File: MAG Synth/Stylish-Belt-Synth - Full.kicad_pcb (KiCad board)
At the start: 2 copper layers, 177.8 x 101.7 mm, 42 parts, among them J1 Conn_01x06, J26 WRITE PATCH, J27 PARAM SELECT, J28 PATCH SELECT, J29 MODE, J30 STYLUS, SW1 Power, U1 stm32f103c8t6-module-china_smd, U2 XPT8871

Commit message: Code now lets you play music!
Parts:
- LS1: footprint Pin_Headers:Pin_Header_Angled_1x02_Pitch2.54mm -> Pin_Headers:Pin_Header_Straight_1x02_Pitch2.54mm
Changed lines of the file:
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@@
   (general
     (thickness 1.6)
-    (drawings 148)
+    (drawings 150)
     (tracks 1041)
     (zones 0)
@@
     (37 F.SilkS user)
     (38 B.Mask user)
-    (39 F.Mask user hide)
+    (39 F.Mask user)
     (40 Dwgs.User user)
     (41 Cmts.User user)
@@
   )
   (setup
-    (last_trace_width 0.762)
+    (last_trace_width 0.508)
     (user_trace_width 0.381)
     (user_trace_width 0.508)
@@
     (add_net "Net-(U1-Pad38)")
   )
+  (module Pin_Headers:Pin_Header_Straight_1x02_Pitch2.54mm (layer F.Cu)
+    (at 196.215 87.63 180)
+    (descr "Through hole straight pin header, 1x02, 2.54mm pitch, single row")
+    (tags "Through hole pin header THT 1x02 2.54mm single row")
+    (fp_text reference LS1 (at 2.54 1.27 90) (layer B.SilkS)
+      (effects (font (size 1 1) (thickness 0.15)) (justify mirror))
+    )
+    (fp_text value Speaker (at 2.54 -3.81 180) (layer B.Fab)
+      (effects (font (size 1.499997 1.499997) (thickness 0.15)) (justify mirror))
+    )
+    (fp_line (start -0.635 -1.27) (end 1.27 -1.27) (layer F.Fab) (width 0.1))
+    (fp_line (start 1.27 -1.27) (end 1.27 3.81) (layer F.Fab) (width 0.1))
+    (fp_line (start 1.27 3.81) (end -1.27 3.81) (layer F.Fab) (width 0.1))
+    (fp_line (start -1.27 3.81) (end -1.27 -0.635) (layer F.Fab) (width 0.1))
+    (fp_line (start -1.27 -0.635) (end -0.635 -1.27) (layer F.Fab) (width 0.1))
+    (fp_line (start -1.33 3.87) (end 1.33 3.87) (layer F.SilkS) (width 0.12))
+    (fp_line (start -1.33 1.27) (end -1.33 3.87) (layer F.SilkS) (width 0.12))
+    (fp_line (start 1.33 1.27) (end 1.33 3.87) (layer F.SilkS) (width 0.12))
+    (fp_line (start -1.33 1.27) (end 1.33 1.27) (layer F.SilkS) (width 0.12))
+    (fp_line (start -1.33 0) (end -1.33 -1.33) (layer F.SilkS) (width 0.12))
+    (fp_line (start -1.33 -1.33) (end 0 -1.33) (layer F.SilkS) (width 0.12))
+    (fp_line (start -1.8 -1.8) (end -1.8 4.35) (layer F.CrtYd) (width 0.05))
+    (fp_line (start -1.8 4.35) (end 1.8 4.35) (layer F.CrtYd) (width 0.05))
+    (fp_line (start 1.8 4.35) (end 1.8 -1.8) (layer F.CrtYd) (width 0.05))
+    (fp_line (start 1.8 -1.8) (end -1.8 -1.8) (layer F.CrtYd) (width 0.05))
+    (fp_text user %R (at 2.77 1.27 90) (layer B.Fab)
+      (effects (font (size 1 1) (thickness 0.15)) (justify mirror))
+    )
+    (pad 1 thru_hole rect (at 0 0 180) (size 1.7 1.7) (drill 1) (layers *.Cu *.Mask)
+      (net 50 /XH-M125-amp-board/OUT+))
+    (pad 2 thru_hole oval (at 0 2.54 180) (size 1.7 1.7) (drill 1) (layers *.Cu *.Mask)
+      (net 48 /XH-M125-amp-board/OUT-))
+    (model ${KISYS3DMOD}/Pin_Headers.3dshapes/Pin_Header_Straight_1x02_Pitch2.54mm.wrl
+      (at (xyz 0 0 0))
+      (scale (xyz 1 1 1))
+      (rotate (xyz 0 0 0))
+    )
+  )
   (module SoftEggKiCAD:LargeRoundTouchPad (layer B.Cu)
     (at 90.932 140.208)
@@
     )
   )
-  (module Pin_Headers:Pin_Header_Angled_1x02_Pitch2.54mm (layer F.Cu)
-    (at 196.215 87.63 180)
-    (descr "Through hole angled pin header, 1x02, 2.54mm pitch, 6mm pin length, single row")
-    (tags "Through hole angled pin header THT 1x02 2.54mm single row")
-    (fp_text reference LS1 (at 2.54 1.27 90) (layer B.SilkS)
-      (effects (font (size 1 1) (thickness 0.15)) (justify mirror))
-    )
-    (fp_text value Speaker (at 2.54 -3.81 180) (layer B.Fab)
-      (effects (font (size 1.499997 1.499997) (thickness 0.15)) (justify mirror))
-    )
-    (fp_line (start 2.135 -1.27) (end 4.04 -1.27) (layer F.Fab) (width 0.1))
-    (fp_line (start 4.04 -1.27) (end 4.04 3.81) (layer F.Fab) (width 0.1))
-    (fp_line (start 4.04 3.81) (end 1.5 3.81) (layer F.Fab) (width 0.1))
-    (fp_line (start 1.5 3.81) (end 1.5 -0.635) (layer F.Fab) (width 0.1))
-    (fp_line (start 1.5 -0.635) (end 2.135 -1.27) (layer F.Fab) (width 0.1))
-    (fp_line (start -0.32 -0.32) (end 1.5 -0.32) (layer F.Fab) (width 0.1))
-    (fp_line (start -0.32 -0.32) (end -0.32 0.32) (layer F.Fab) (width 0.1))
-    (fp_line (start -0.32 0.32) (end 1.5 0.32) (layer F.Fab) (width 0.1))
-    (fp_line (start 4.04 -0.32) (end 10.04 -0.32) (layer F.Fab) (width 0.1))
-    (fp_line (start 10.04 -0.32) (end 10.04 0.32) (layer F.Fab) (width 0.1))
-    (fp_line (start 4.04 0.32) (end 10.04 0.32) (layer F.Fab) (width 0.1))
-    (fp_line (start -0.32 2.22) (end 1.5 2.22) (layer F.Fab) (width 0.1))
-    (fp_line (start -0.32 2.22) (end -0.32 2.86) (layer F.Fab) (width 0.1))
-    (fp_line (start -0.32 2.86) (end 1.5 2.86) (layer F.Fab) (width 0.1))
-    (fp_line (start 4.04 2.22) (end 10.04 2.22) (layer F.Fab) (width 0.1))
-    (fp_line (start 10.04 2.22) (end 10.04 2.86) (layer F.Fab) (width 0.1))
-    (fp_line (start 4.04 2.86) (end 10.04 2.86) (layer F.Fab) (width 0.1))
-    (fp_line (start 1.44 -1.33) (end 1.44 3.87) (layer F.SilkS) (width 0.12))
-    (fp_line (start 1.44 3.87) (end 4.1 3.87) (layer F.SilkS) (width 0.12))
-    (fp_line (start 4.1 3.87) (end 4.1 -1.33) (layer F.SilkS) (width 0.12))
-    (fp_line (start 4.1 -1.33) (end 1.44 -1.33) (layer F.SilkS) (width 0.12))
-    (fp_line (start 4.1 -0.38) (end 10.1 -0.38) (layer F.SilkS) (width 0.12))
-    (fp_line (start 10.1 -0.38) (end 10.1 0.38) (layer F.SilkS) (width 0.12))
-    (fp_line (start 10.1 0.38) (end 4.1 0.38) (layer F.SilkS) (width 0.12))
-    (fp_line (start 4.1 -0.32) (end 10.1 -0.32) (layer F.SilkS) (width 0.12))
-    (fp_line (start 4.1 -0.2) (end 10.1 -0.2) (layer F.SilkS) (width 0.12))
-    (fp_line (start 4.1 -0.08) (end 10.1 -0.08) (layer F.SilkS) (width 0.12))
-    (fp_line (start 4.1 0.04) (end 10.1 0.04) (layer F.SilkS) (width 0.12))
-    (fp_line (start 4.1 0.16) (end 10.1 0.16) (layer F.SilkS) (width 0.12))
-    (fp_line (start 4.1 0.28) (end 10.1 0.28) (layer F.SilkS) (width 0.12))
-    (fp_line (start 1.11 -0.38) (end 1.44 -0.38) (layer F.SilkS) (width 0.12))
-    (fp_line (start 1.11 0.38) (end 1.44 0.38) (layer F.SilkS) (width 0.12))
-    (fp_line (start 1.44 1.27) (end 4.1 1.27) (layer F.SilkS) (width 0.12))
-    (fp_line (start 4.1 2.16) (end 10.1 2.16) (layer F.SilkS) (width 0.12))
-    (fp_line (start 10.1 2.16) (end 10.1 2.92) (layer F.SilkS) (width 0.12))
-    (fp_line (start 10.1 2.92) (end 4.1 2.92) (layer F.SilkS) (width 0.12))
-    (fp_line (start 1.042929 2.16) (end 1.44 2.16) (layer F.SilkS) (width 0.12))
-    (fp_line (start 1.042929 2.92) (end 1.44 2.92) (layer F.SilkS) (width 0.12))
-    (fp_line (start -1.27 0) (end -1.27 -1.27) (layer F.SilkS) (width 0.12))
-    (fp_line (start -1.27 -1.27) (end 0 -1.27) (layer F.SilkS) (width 0.12))
-    (fp_line (start -1.8 -1.8) (end -1.8 4.35) (layer F.CrtYd) (width 0.05))
-    (fp_line (start -1.8 4.35) (end 10.55 4.35) (layer F.CrtYd) (width 0.05))
-    (fp_line (start 10.55 4.35) (end 10.55 -1.8) (layer F.CrtYd) (width 0.05))
-    (fp_line (start 10.55 -1.8) (end -1.8 -1.8) (layer F.CrtYd) (width 0.05))
-    (fp_text user %R (at 2.77 1.27 90) (layer B.Fab)
-      (effects (font (size 1 1) (thickness 0.15)) (justify mirror))
-    )
-    (pad 1 thru_hole rect (at 0 0 180) (size 1.7 1.7) (drill 1) (layers *.Cu *.Mask)
-      (net 50 /XH-M125-amp-board/OUT+))
-    (pad 2 thru_hole oval (at 0 2.54 180) (size 1.7 1.7) (drill 1) (layers *.Cu *.Mask)
-      (net 48 /XH-M125-amp-board/OUT-))
-    (model ${KISYS3DMOD}/Pin_Headers.3dshapes/Pin_Header_Angled_1x02_Pitch2.54mm.wrl
-      (offset (xyz 0.127 -2.54 -1.6764))
-      (scale (xyz 1 1 1))
-      (rotate (xyz 180 0 0))
-    )
-  )
   (module WS2812B (layer F.Cu)
     (at 123.825 96.139 202.5)
@@
     (descr "<b>Intelligent control LED with integrated light source</b><p>WS2812B<br>source: http://www.world-semi.com/uploads/soft/130904/1_1500205981.pdf")
     (attr smd)
-    (fp_text reference D0 (at 6.307 -1.71371 90) (layer F.SilkS)
+    (fp_text reference D0 (at 2.4003 -3.556 90) (layer F.SilkS)
       (effects (font (size 0.802674 0.802674) (thickness 0.05)))
     )
-    (fp_text value WS2812B (at 5.78549 1.29688 90) (layer F.SilkS)
+    (fp_text value WS2812B (at 4.0259 -0.0381 180) (layer F.SilkS)
       (effects (font (size 0.480622 0.480622) (thickness 0.05)))
     )
@@
       (xy 6.050594 -4.164124)) (layer F.SilkS) (width 0.01))
   )
+  (gr_text Stylish! (at 189.6364 67.1957) (layer F.Mask)
+    (effects (font (size 5.08 5.08) (thickness 1.27)))
+  )
+  (gr_text Stylish! (at 189.4586 66.9544) (layer F.SilkS)
+    (effects (font (size 5.08 5.08) (thickness 0.762)))
+  )
   (gr_text MODE (at 111.125 88.9) (layer F.Mask)
     (effects (font (size 1.5 1.5) (thickness 0.3)))
@@
     (effects (font (size 1.5 1.5) (thickness 0.3)))
   )
-  (gr_text GND (at 180.975 59.69) (layer F.Cu)
+  (gr_text GND (at 175.5013 59.8043) (layer F.Cu)
     (effects (font (size 1.5 1.5) (thickness 0.3)))
   )

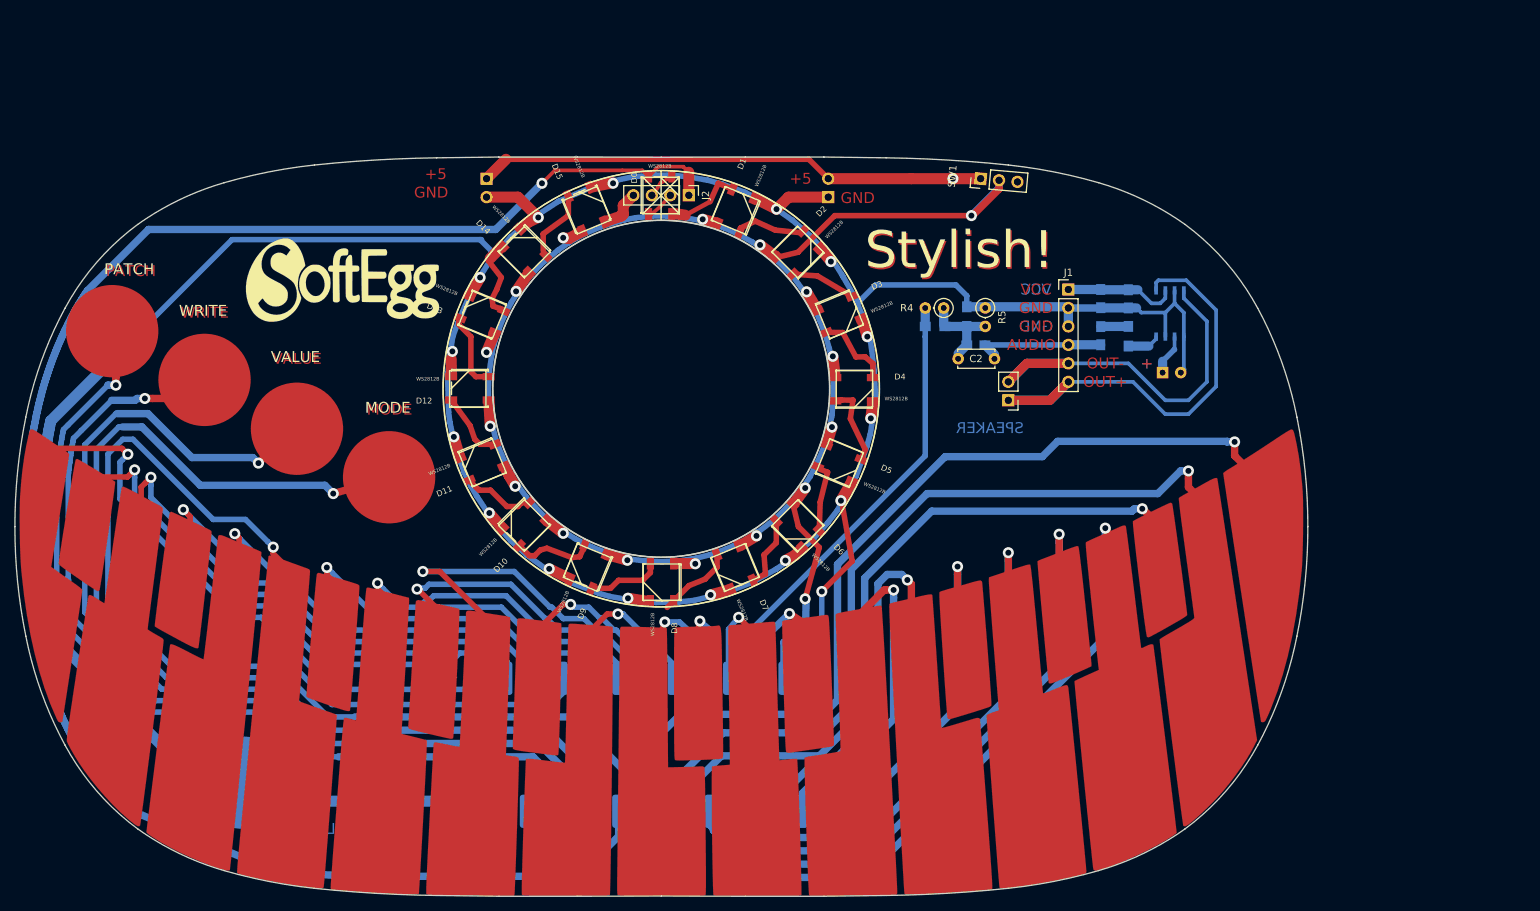
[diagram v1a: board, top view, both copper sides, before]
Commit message: 1st draft of case. Updates to PCB for battery holder mounting and other stuff. Gerbers added for Tindie. Updates to source code, although I don't know if they are the in progress state machine updates or not.
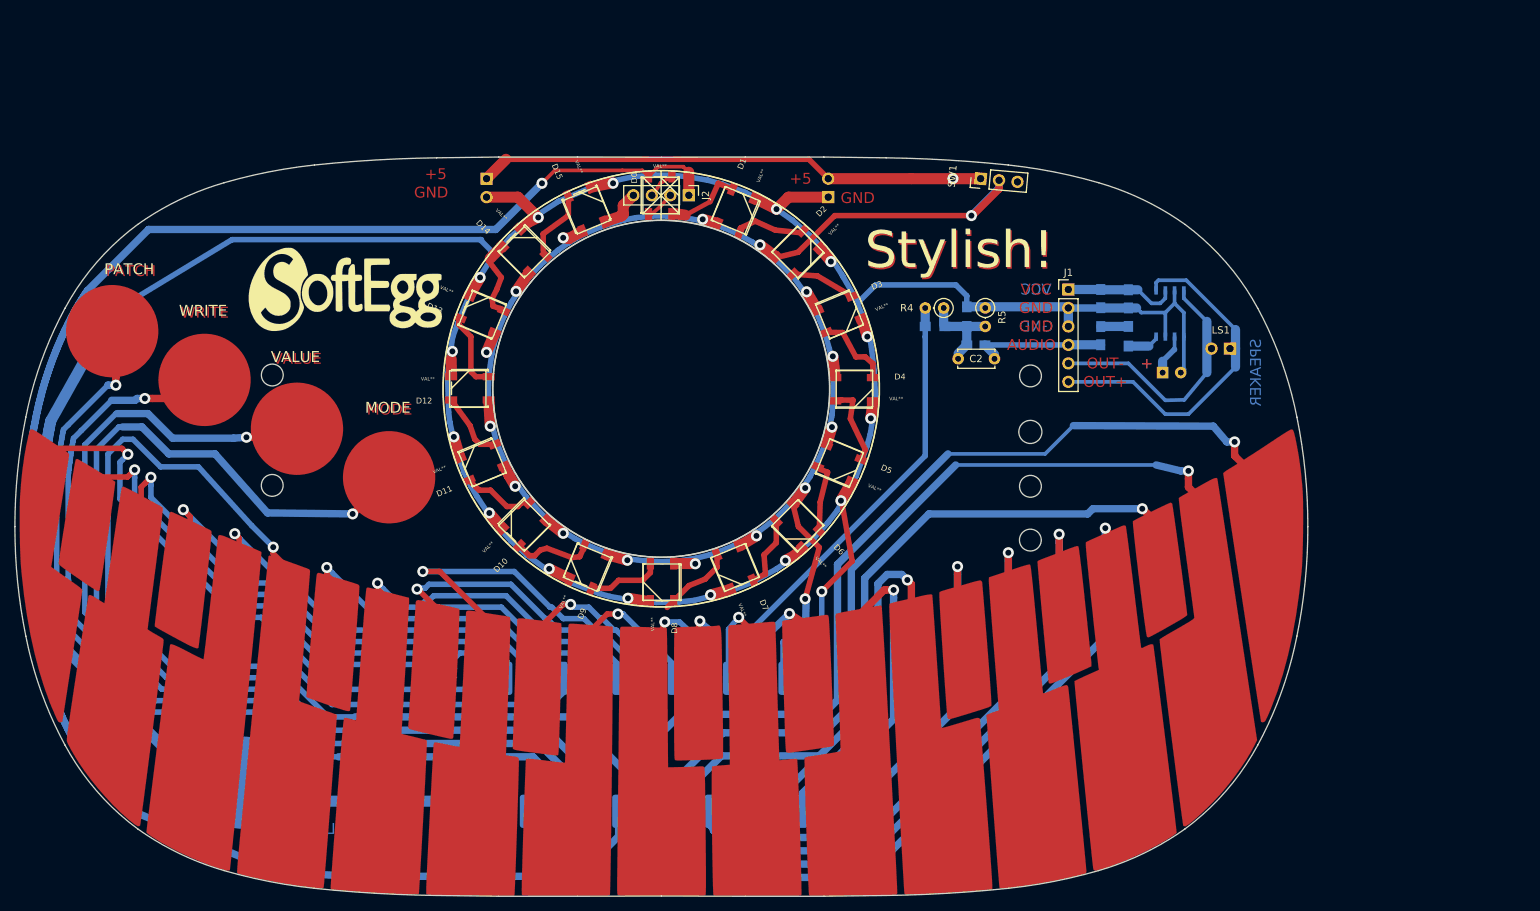
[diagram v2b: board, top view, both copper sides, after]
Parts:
- added REF**: AA Battery Holder, SoftEggKiCAD:AA_Battery_Holder_SoftEgg, B.Cu at (95.0, 91.9)
- added REF**: AA Battery Holder, SoftEggKiCAD:AA_Battery_Holder_SoftEgg, B.Cu at (199.3, 92.1)
- D0, D1, D10, D11, D12, D13, D14, D15, D2, D3, D4, D5, D6, D7, D8, D9: value WS2812B -> VAL**; footprint WS2812B -> WS2812B:WS2812B
- LS1: moved to B.Cu
- moved LS1 31.3 mm to (226.7, 80.5), turned to 90 degrees
- moved G*** 1.33 mm to (105.0, 72.4)
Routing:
- net /XH-M125-amp-board/OUT-: track 54.7 -> 35.5 mm
- net /XH-M125-amp-board/OUT+: track 64.0 -> 49.9 mm
- net Net-(J27-Pad1): track 141.7 -> 138.6 mm
- net Net-(J29-Pad1): track 154.3 -> 157.4 mm
- net Net-(KB1-Pad24): track 120.3 -> 122.0 mm
- net /WS2812B-16-LED-RING/GND: track 513.2 -> 514.4 mm

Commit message: New power switch. 3d model included. 3d model of the amp board included. PCB redesign in progress.
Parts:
- removed C2: 1uF, Capacitors_ThroughHole:C_Disc_D5.0mm_W2.5mm_P5.00mm
- removed C4: 470uF, Capacitors_SMD:C_0805_HandSoldering
- removed C5: 1uF, Capacitors_SMD:C_0805_HandSoldering
- removed C6: 1uF, Capacitors_ThroughHole:CP_Radial_Tantal_D4.5mm_P2.50mm
- removed C7: 0.39uF, Capacitors_SMD:C_0805_HandSoldering
- removed R4: 10k, Resistors_ThroughHole:R_Axial_DIN0207_L6.3mm_D2.5mm_P2.54mm_Vertical
- removed R5: 1k, Resistors_ThroughHole:R_Axial_DIN0207_L6.3mm_D2.5mm_P2.54mm_Vertical
- added CA1: 470uF, SoftEggKiCAD:C_Disc_D5.0mm_W2.5mm_P5.00mm+SMD, B.Cu at (197.6, 88.9)
- added CA2: 1uF, SoftEggKiCAD:C_Disc_D5.0mm_W2.5mm_P5.00mm+SMD, B.Cu at (197.6, 85.3)
- added CA3: 1uF, Capacitors_ThroughHole:CP_Radial_Tantal_D4.5mm_P2.50mm, B.Cu at (189.5, 97.0)
- added CA4: 0.39uF, SoftEggKiCAD:C_Disc_D5.0mm_W2.5mm_P5.00mm+SMD, B.Cu at (183.4, 84.8)
- added CL0: 104, Capacitors_SMD:C_0805_HandSoldering, B.Cu at (142.0, 60.4)
- added CL1: 104, Capacitors_SMD:C_0805_HandSoldering, B.Cu at (158.5, 61.6)
- added CL10: 104, Capacitors_SMD:C_0805_HandSoldering, B.Cu at (129.5, 104.6)
- added CL11: 104, Capacitors_SMD:C_0805_HandSoldering, B.Cu at (123.7, 96.0)
- added CL12: 104, Capacitors_SMD:C_0805_HandSoldering, B.Cu at (121.9, 85.9)
- added CL13: 104, Capacitors_SMD:C_0805_HandSoldering, B.Cu at (123.6, 75.8)
- added CL14: 104, Capacitors_SMD:C_0805_HandSoldering, B.Cu at (129.7, 67.1)
- added CL15: 104, Capacitors_SMD:C_0805_HandSoldering, B.Cu at (138.2, 61.5)
- added CL2: 104, Capacitors_SMD:C_0805_HandSoldering, B.Cu at (167.4, 67.3)
- added CL3: 104, Capacitors_SMD:C_0805_HandSoldering, B.Cu at (173.0, 75.7)
- added CL4: 104, Capacitors_SMD:C_0805_HandSoldering, B.Cu at (175.1, 86.1)
- added CL5: 104, Capacitors_SMD:C_0805_HandSoldering, B.Cu at (172.9, 96.3)
- added CL6: 104, Capacitors_SMD:C_0805_HandSoldering, B.Cu at (167.2, 104.8)
- added CL7: 104, Capacitors_SMD:C_0805_HandSoldering, B.Cu at (158.3, 110.7)
- added CL8: 104, Capacitors_SMD:C_0805_HandSoldering, B.Cu at (148.6, 112.7)
- added CL9: 104, Capacitors_SMD:C_0805_HandSoldering, B.Cu at (138.3, 110.5)
- added D1: 1N4148, SoftEggKiCAD:D_DO-35_SOD27_P7.62mm_Horizontal+SMD, F.Cu at (116.1, 91.7)
- added D2: 1N4148, SoftEggKiCAD:D_DO-35_SOD27_P7.62mm_Horizontal+SMD, F.Cu at (106.2, 105.2)
- added J0: USB_B, Connectors:USB_B, B.Cu at (119.8, 62.4)
- added JA1: Conn_01x06, Pin_Headers:Pin_Header_Straight_1x06_Pitch2.54mm, F.Cu at (196.1, 81.8)
- BT1, BT2: footprint Pin_Headers:Pin_Header_Angled_1x02_Pitch2.54mm -> Pin_Headers:Pin_Header_Straight_1x02_Pitch2.54mm
- C1: footprint Capacitors_SMD:C_0805_HandSoldering -> SoftEggKiCAD:C_Disc_D5.0mm_W2.5mm_P5.00mm+SMD
- J1: value Conn_01x06 -> Audio-Jack-3_2Switches; footprint Pin_Headers:Pin_Header_Straight_1x06_Pitch2.54mm -> Connectors:PJ320E_3.5mm_Jack
- R1, R2, R3: footprint Resistors_SMD:R_0805_HandSoldering -> SoftEggKiCAD:R_Axial_DIN0204_L3.6mm_D1.6mm_P7.62mm_Horizontal+SMD804
- RGB0: renamed from D0; value VAL** -> WS2812B
- RGB1: renamed from D1; value VAL** -> WS2812B
- RGB10: renamed from D10; value VAL** -> WS2812B
- RGB11: renamed from D11; value VAL** -> WS2812B
- RGB12: renamed from D12; value VAL** -> WS2812B
- RGB13: renamed from D13; value VAL** -> WS2812B
- RGB14: renamed from D14; value VAL** -> WS2812B
- RGB15: renamed from D15; value VAL** -> WS2812B
- RGB2: renamed from D2; value VAL** -> WS2812B
- RGB3: renamed from D3; value VAL** -> WS2812B
- RGB4: renamed from D4; value VAL** -> WS2812B
- RGB5: renamed from D5; value VAL** -> WS2812B
- RGB6: renamed from D6; value VAL** -> WS2812B
- RGB7: renamed from D7; value VAL** -> WS2812B
- RGB8: renamed from D8; value VAL** -> WS2812B
- RGB9: renamed from D9; value VAL** -> WS2812B
- SW1: footprint Pin_Headers:Pin_Header_Straight_1x03_Pitch2.54mm -> SVTmaker:MSS22D18+THT
- U1: value stm32f103c8t6-module-china_smd -> stm32f103c8t6-module-china
- moved BT1 104.3 mm to (228.6, 62.5), turned to 0 degrees
- moved BT2 60.7 mm to (232.2, 59.9), turned to 180 degrees
- moved LS1 40.5 mm to (191.0, 61.5), turned to 0 degrees
- moved J30 33.1 mm to (122.3, 150.7)
- moved U2 31.6 mm to (195.1, 97.0), turned to 0 degrees
- moved J1 27.3 mm to (178.8, 63.0)
- moved R3 24.9 mm to (190.0, 88.9), turned to 180 degrees
- moved REF** 20.3 mm to (215.1, 104.8)
- moved REF** 17.5 mm to (82.9, 104.6)
- moved SW1 16.3 mm to (205.7, 66.5), turned to 180 degrees
- moved R2 10.8 mm to (179.8, 74.2), turned to 0 degrees
- moved C1 1.78 mm to (190.5, 78.7), turned to 90 degrees
- moved R1 1.19 mm to (187.3, 77.5)
- renumbered J2 to JL1
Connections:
- net /WS2812B-16-LED-RING/DIN renamed /LED_DIN
- net AUDIO_OUT renamed /AUDIO_OUT
- net Net-(J26-Pad1) renamed /WRITE
- net Net-(J27-Pad1) renamed /PARAM
- net Net-(J28-Pad1) renamed /PATCH
- net Net-(KB1-Pad0) renamed /C0
- net Net-(KB1-Pad1) renamed /C#0
- net Net-(KB1-Pad10) renamed /A#0
- net Net-(KB1-Pad11) renamed /B0
- net Net-(KB1-Pad12) renamed /C1
- net Net-(KB1-Pad13) renamed /C#1
- net Net-(KB1-Pad14) renamed /D1
- net Net-(KB1-Pad15) renamed /D#1
- net Net-(KB1-Pad16) renamed /E1
- net Net-(KB1-Pad17) renamed /F1
- net Net-(KB1-Pad18) renamed /F#1
- net Net-(KB1-Pad19) renamed /G1
- net Net-(KB1-Pad2) renamed /D0
- net Net-(KB1-Pad20) renamed /G#1
- net Net-(KB1-Pad21) renamed /A1
- net Net-(KB1-Pad22) renamed /A#1
- net Net-(KB1-Pad23) renamed /B1
- net Net-(KB1-Pad24) renamed /C2
- net Net-(KB1-Pad3) renamed /D#0
- net Net-(KB1-Pad4) renamed /E0
- net Net-(KB1-Pad5) renamed /F0
- net Net-(KB1-Pad6) renamed /F#0
- net Net-(KB1-Pad9) renamed /A0
- BT1 pad 2: /WS2812B-16-LED-RING/GND -> GND
- BT2 pad 1: /WS2812B-16-LED-RING/GND -> GND
- C1 pad 1: /PWM_Audio_Out -> /PWM_OUT
- J1 pad 1: /XH-M125-amp-board/VCC -> /XH-M125-amp-board/OUT+
- J1 pad 2: /WS2812B-16-LED-RING/GND -> /XH-M125-amp-board/OUT+
- J1 pad 3: /WS2812B-16-LED-RING/GND -> /XH-M125-amp-board/OUT-
- J1 pad 4: /PWM_Audio_Out -> Net-(J1-Pad4)
- J1 pad 5: /XH-M125-amp-board/OUT- -> Net-(J1-Pad4)
- J29 pad 1: Net-(J29-Pad1) -> Net-(BD1-Pad1)
- J30 pad 1: /WS2812B-16-LED-RING/GND -> GND
- JL1 pad 2: /WS2812B-16-LED-RING/5V -> /+5V
- JL1 pad 3: /WS2812B-16-LED-RING/GND -> GND
- KB1 pad 7: Net-(KB1-Pad7) -> /G0
- KB1 pad 8: Net-(KB1-Pad8) -> /G#0
- LS1 pad 1: /XH-M125-amp-board/OUT+ -> Net-(J1-Pad4)
- R2 pad 1: /WS2812B-16-LED-RING/GND -> GND
- RGB0 pad 1: /WS2812B-16-LED-RING/5V -> /+5V
- RGB0 pad 3: /WS2812B-16-LED-RING/GND -> GND
- RGB1 pad 1: /WS2812B-16-LED-RING/5V -> /+5V
- RGB1 pad 3: /WS2812B-16-LED-RING/GND -> GND
- RGB10 pad 1: /WS2812B-16-LED-RING/5V -> /+5V
- RGB10 pad 3: /WS2812B-16-LED-RING/GND -> GND
- RGB11 pad 1: /WS2812B-16-LED-RING/5V -> /+5V
- RGB11 pad 3: /WS2812B-16-LED-RING/GND -> GND
- RGB12 pad 1: /WS2812B-16-LED-RING/5V -> /+5V
- RGB12 pad 3: /WS2812B-16-LED-RING/GND -> GND
- RGB13 pad 1: /WS2812B-16-LED-RING/5V -> /+5V
- RGB13 pad 3: /WS2812B-16-LED-RING/GND -> GND
- RGB14 pad 1: /WS2812B-16-LED-RING/5V -> /+5V
- RGB14 pad 3: /WS2812B-16-LED-RING/GND -> GND
- RGB15 pad 1: /WS2812B-16-LED-RING/5V -> /+5V
- RGB15 pad 3: /WS2812B-16-LED-RING/GND -> GND
- RGB2 pad 1: /WS2812B-16-LED-RING/5V -> /+5V
- RGB2 pad 3: /WS2812B-16-LED-RING/GND -> GND
- RGB3 pad 1: /WS2812B-16-LED-RING/5V -> /+5V
- RGB3 pad 3: /WS2812B-16-LED-RING/GND -> GND
- RGB4 pad 1: /WS2812B-16-LED-RING/5V -> /+5V
- RGB4 pad 3: /WS2812B-16-LED-RING/GND -> GND
- RGB5 pad 1: /WS2812B-16-LED-RING/5V -> /+5V
- RGB5 pad 3: /WS2812B-16-LED-RING/GND -> GND
- RGB6 pad 1: /WS2812B-16-LED-RING/5V -> /+5V
- RGB6 pad 3: /WS2812B-16-LED-RING/GND -> GND
- RGB7 pad 1: /WS2812B-16-LED-RING/5V -> /+5V
- RGB7 pad 3: /WS2812B-16-LED-RING/GND -> GND
- RGB8 pad 1: /WS2812B-16-LED-RING/5V -> /+5V
- RGB8 pad 3: /WS2812B-16-LED-RING/GND -> GND
- RGB9 pad 1: /WS2812B-16-LED-RING/5V -> /+5V
- RGB9 pad 3: /WS2812B-16-LED-RING/GND -> GND
- U1 pad 18: /WS2812B-16-LED-RING/5V -> /+5V
- U1 pad 19: /WS2812B-16-LED-RING/GND -> GND
- U1 pad 31: Net-(J29-Pad1) -> /G0
- U1 pad 36: Net-(U1-Pad36) -> /G#0
- U1 pad 39: /WS2812B-16-LED-RING/GND -> GND
- U1 pad 40: /WS2812B-16-LED-RING/GND -> GND
- U1 pad 8: Net-(KB1-Pad7) -> Net-(J0-Pad2)
- U1 pad 9: Net-(KB1-Pad8) -> Net-(J0-Pad3)
- U2 pad 1: /WS2812B-16-LED-RING/GND -> GND
- U2 pad 3: /WS2812B-16-LED-RING/GND -> GND
- U2 pad 6: /XH-M125-amp-board/VCC -> /+5V
- U2 pad 7: /WS2812B-16-LED-RING/GND -> GND
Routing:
- net /WS2812B-16-LED-RING/GND: track 514.4 -> 0.00 mm, vias 16 -> 0
- net GND: track 0.00 -> 360.9 mm, vias 0 -> 13
- net /+5V: track 0.00 -> 275.0 mm, vias 0 -> 16
- net /WS2812B-16-LED-RING/5V: track 263.7 -> 0.00 mm, vias 17 -> 0
- net /G#0: track 0.00 -> 166.6 mm, vias 0 -> 1
- net Net-(J29-Pad1): track 157.4 -> 0.00 mm, vias 1 -> 0
- net /G0: track 0.00 -> 146.7 mm, vias 0 -> 1
- net Net-(J0-Pad3): track 0.00 -> 93.4 mm, vias 0 -> 1
- net Net-(J0-Pad2): track 0.00 -> 92.7 mm, vias 0 -> 1
- net Net-(BT1-Pad1): track 74.0 -> 0.00 mm, vias 1 -> 0
- net Net-(KB1-Pad7): track 42.6 -> 0.00 mm, vias 1 -> 0
- net Net-(KB1-Pad8): track 40.3 -> 0.00 mm, vias 1 -> 0
- net /WRITE: track 127.6 -> 150.8 mm
- net /B1: track 106.4 -> 125.8 mm
- net /PWM_Audio_Out: track 18.4 -> 0.00 mm
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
